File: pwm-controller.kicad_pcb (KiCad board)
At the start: 4 copper layers, 50 x 50 mm, 63 parts, among them J1 DEBUG_ADDRESS_I2C_INT, J2 POWER, J3 OUT+, J4 OUT-, Q1 MMBT5551, Q10 MMBT5551, Q2 SiS402DN, Q3 SiS402DN, Q4 MMBT5401, Q5 MMBT5551, Q6 SiS402DN, Q7 SiS402DN, Q8 MMBT5401, Q9 MMBT5551, SW1 EC12D1524403, U1 STM8S003F3Px, U2 78L05

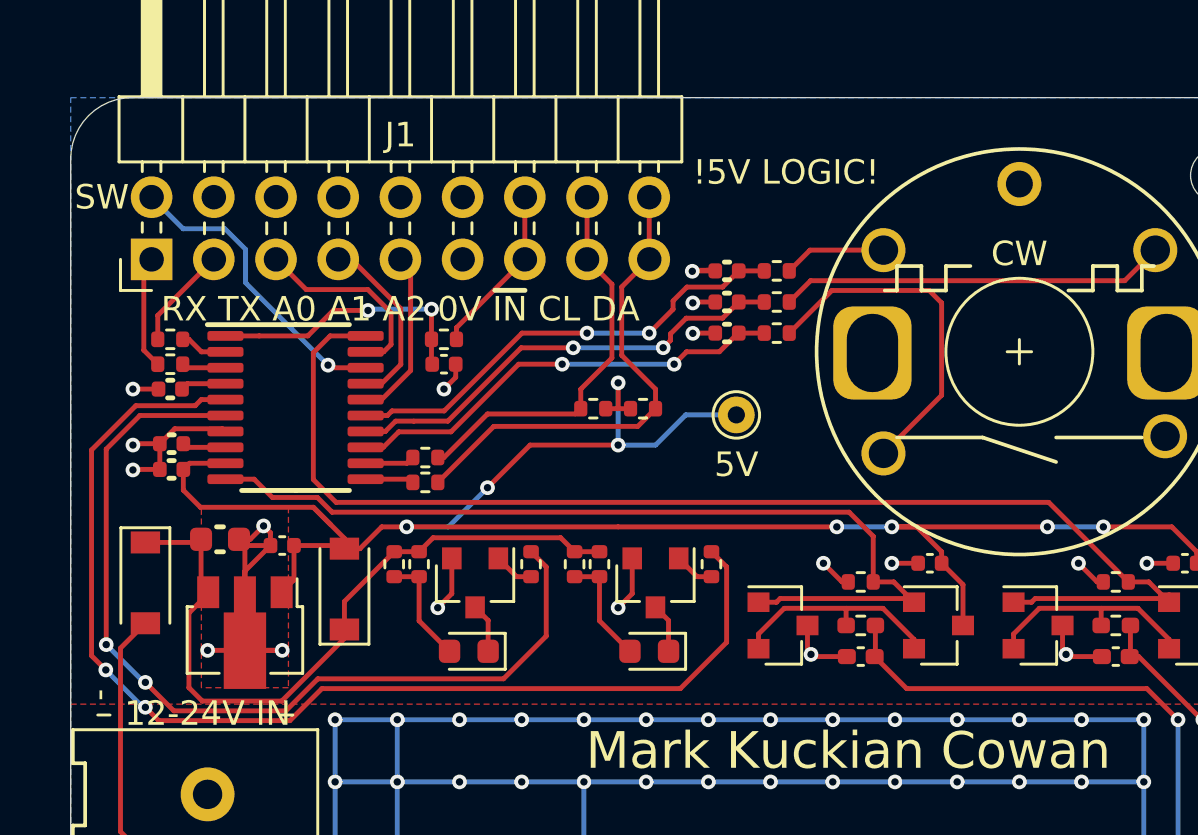
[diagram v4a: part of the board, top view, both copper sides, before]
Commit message: exposed NRST
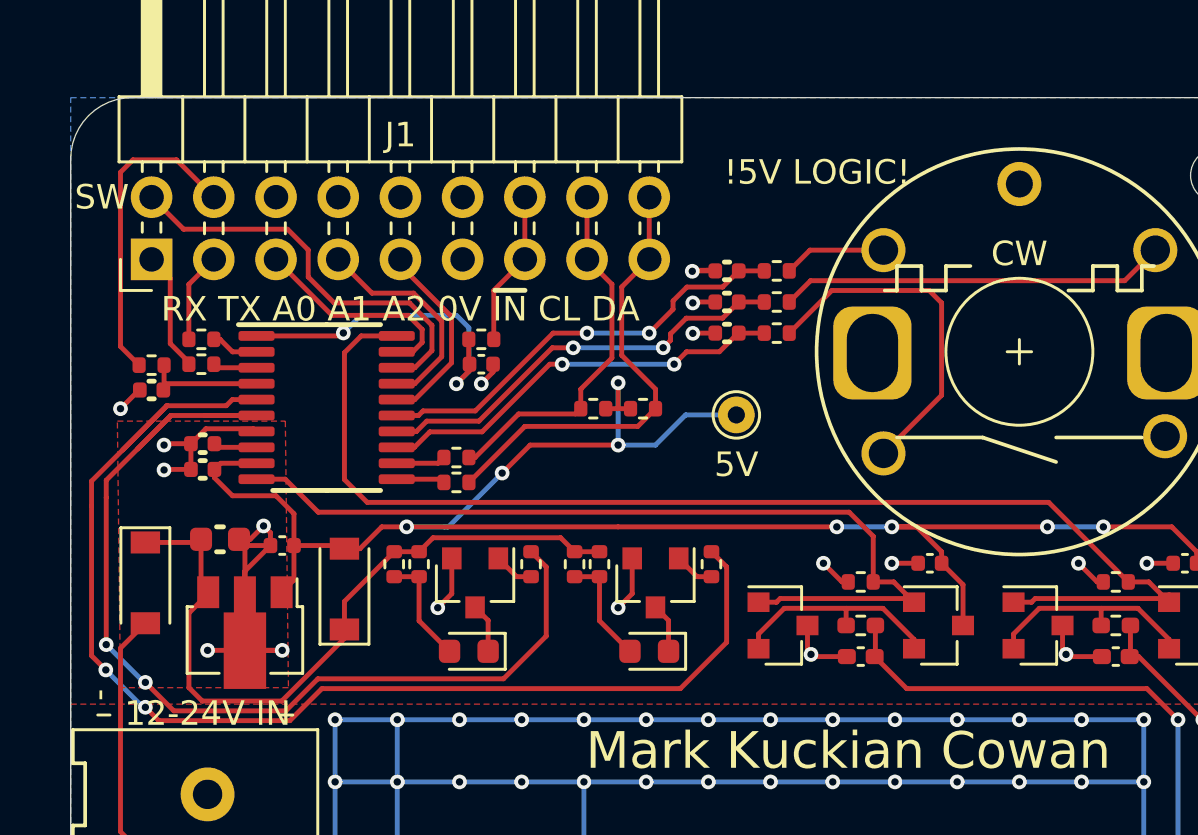
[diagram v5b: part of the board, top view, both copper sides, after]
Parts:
- added R21: 100, Resistor_SMD:R_0402_1005Metric, F.Cu at (79.5, 87.1)
- moved C3 1.52 mm to (93.0, 87.1)
- moved R4 1.52 mm to (93.0, 86.1)
- moved R6 1.27 mm to (81.5, 86.1)
- moved R7 1.27 mm to (81.5, 87.1)
- moved C1 1.27 mm to (81.6, 90.3)
- moved C2 1.27 mm to (81.6, 91.4)
- moved R1 1.27 mm to (91.9, 90.9)
- moved R2 1.27 mm to (91.9, 91.9)
- moved U1 1.27 mm to (86.6, 88.9)
- moved C6 0.76 mm to (79.5, 88.1)
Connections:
- net Net-(C6-Pad1) renamed /NRST_PIN
- J1 pad 4: GND -> NRST
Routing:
- net NRST: track 0.00 -> 12.8 mm
- net SWIM: track 12.4 -> 17.0 mm, vias 1 -> 0
- net LED2: track 37.5 -> 42.0 mm
- net +5V: track 80.5 -> 76.5 mm
- net LED1: track 47.0 -> 50.1 mm
- net /NRST_PIN: track 1.86 -> 4.80 mm
- net /INT_PIN: track 11.1 -> 13.8 mm
- net SADD1: track 7.43 -> 9.56 mm
- net SADD2: track 7.04 -> 8.54 mm
- net PWM1: track 37.8 -> 36.5 mm
- net PWM2: track 51.4 -> 50.1 mm
- net SCL: track 16.2 -> 15.0 mm
- net SDA: track 19.8 -> 18.5 mm
- net RE_B: track 18.2 -> 16.9 mm
- net RE_Q: track 18.6 -> 17.4 mm
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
